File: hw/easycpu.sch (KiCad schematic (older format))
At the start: 0 parts

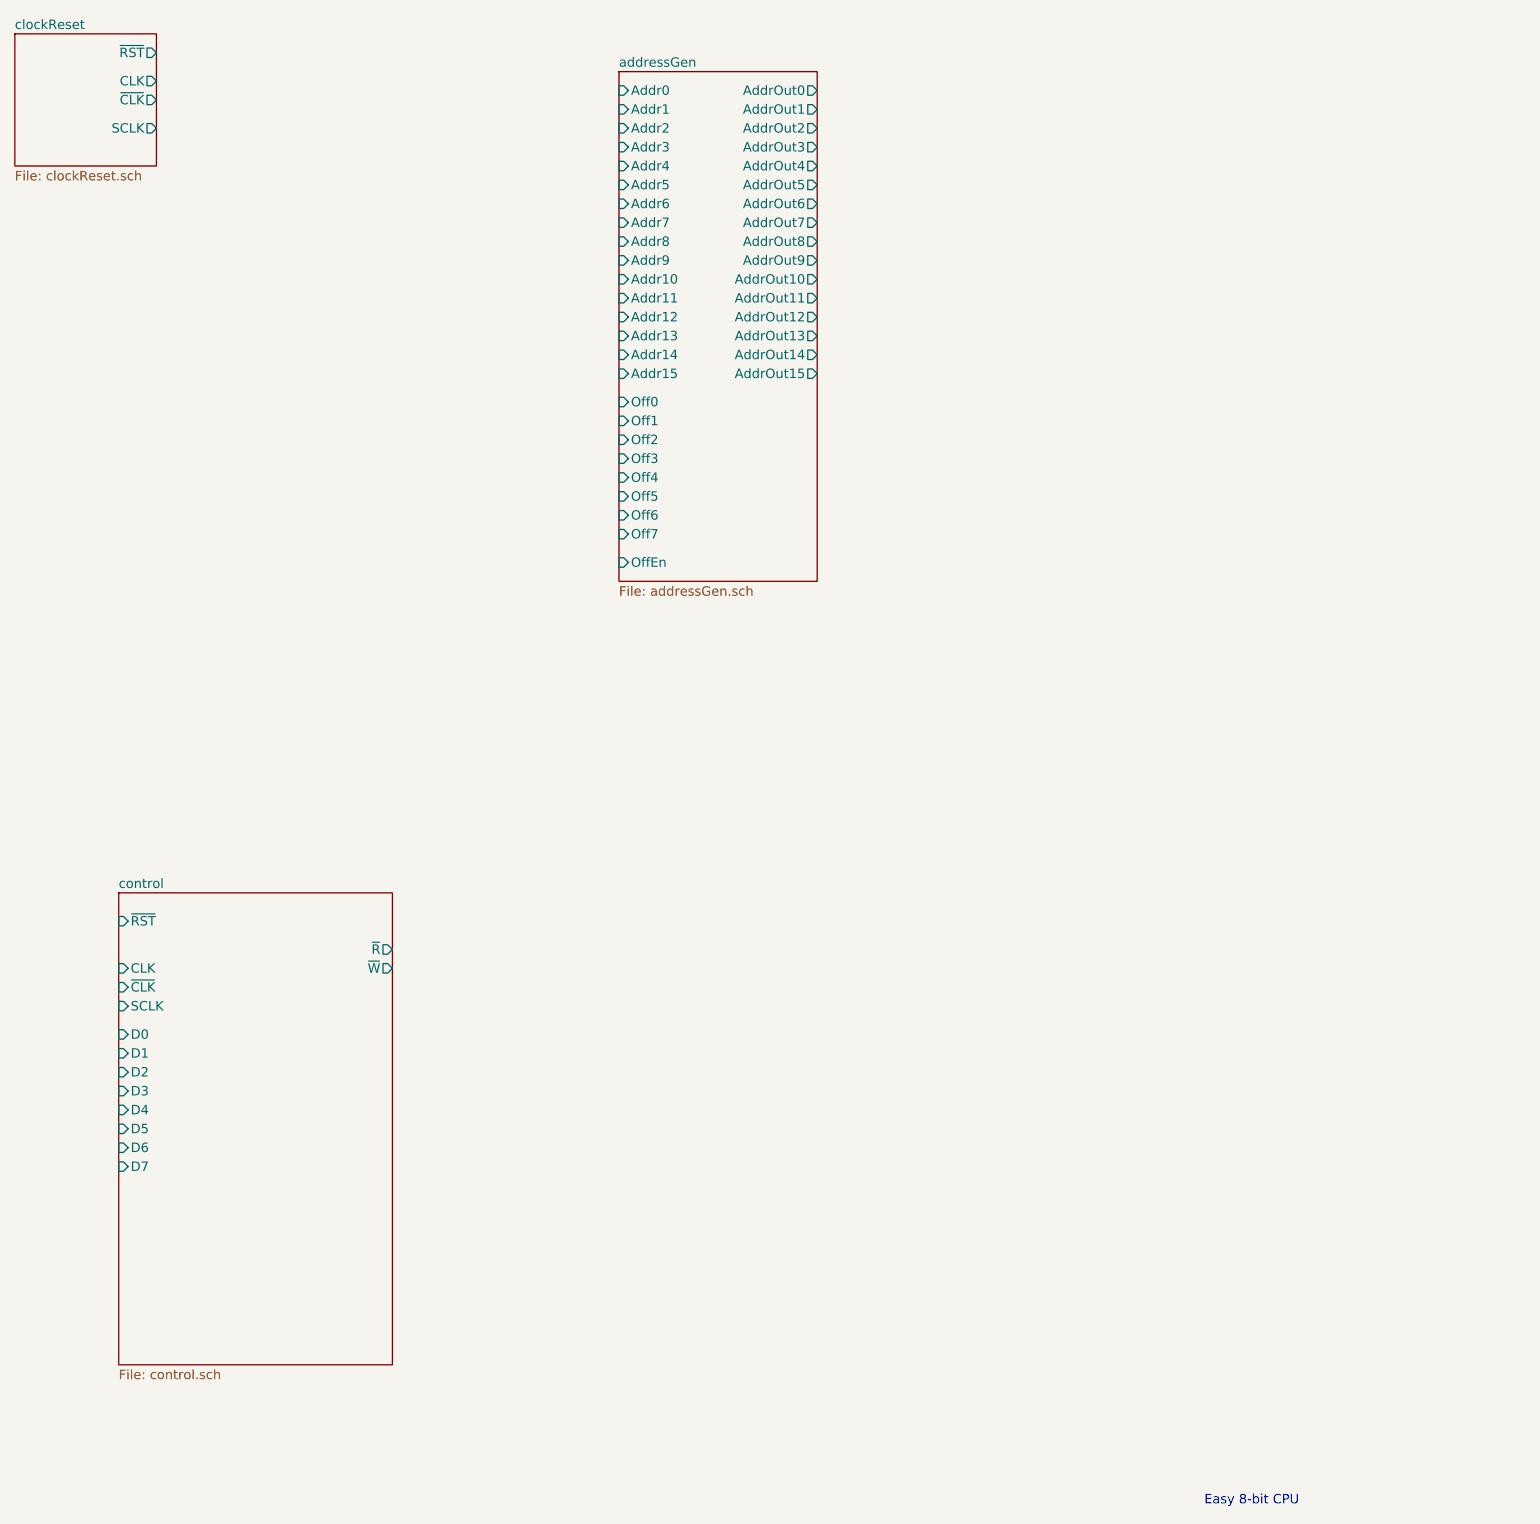
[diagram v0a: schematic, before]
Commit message: use '273 registers for ucode, initial PC design
The microcode registers need to be reset to a known
state on startup.  The 74HCT273 is appropriate for this.
One consequence is that all microcode signals must be
designed such that a 0 is the correct output for
coming out of reset: the main thing that needs to
happen is putting an initial value into the program
counter.  I'm assuming that a '541 buffer will
put an appropriate byte value (maybe 0xC0) on the
D bus on reset, and the PC can load this in both
bytes (so, effective initial PC of 0xC0C0).

Created an initial design for the program counter.
Used 74HC191 synchronous counters, with a 74HC10
triple 3-input NAND to enable counting for each 4
bits as appopriate based on the terminal count status
of the prior counters.
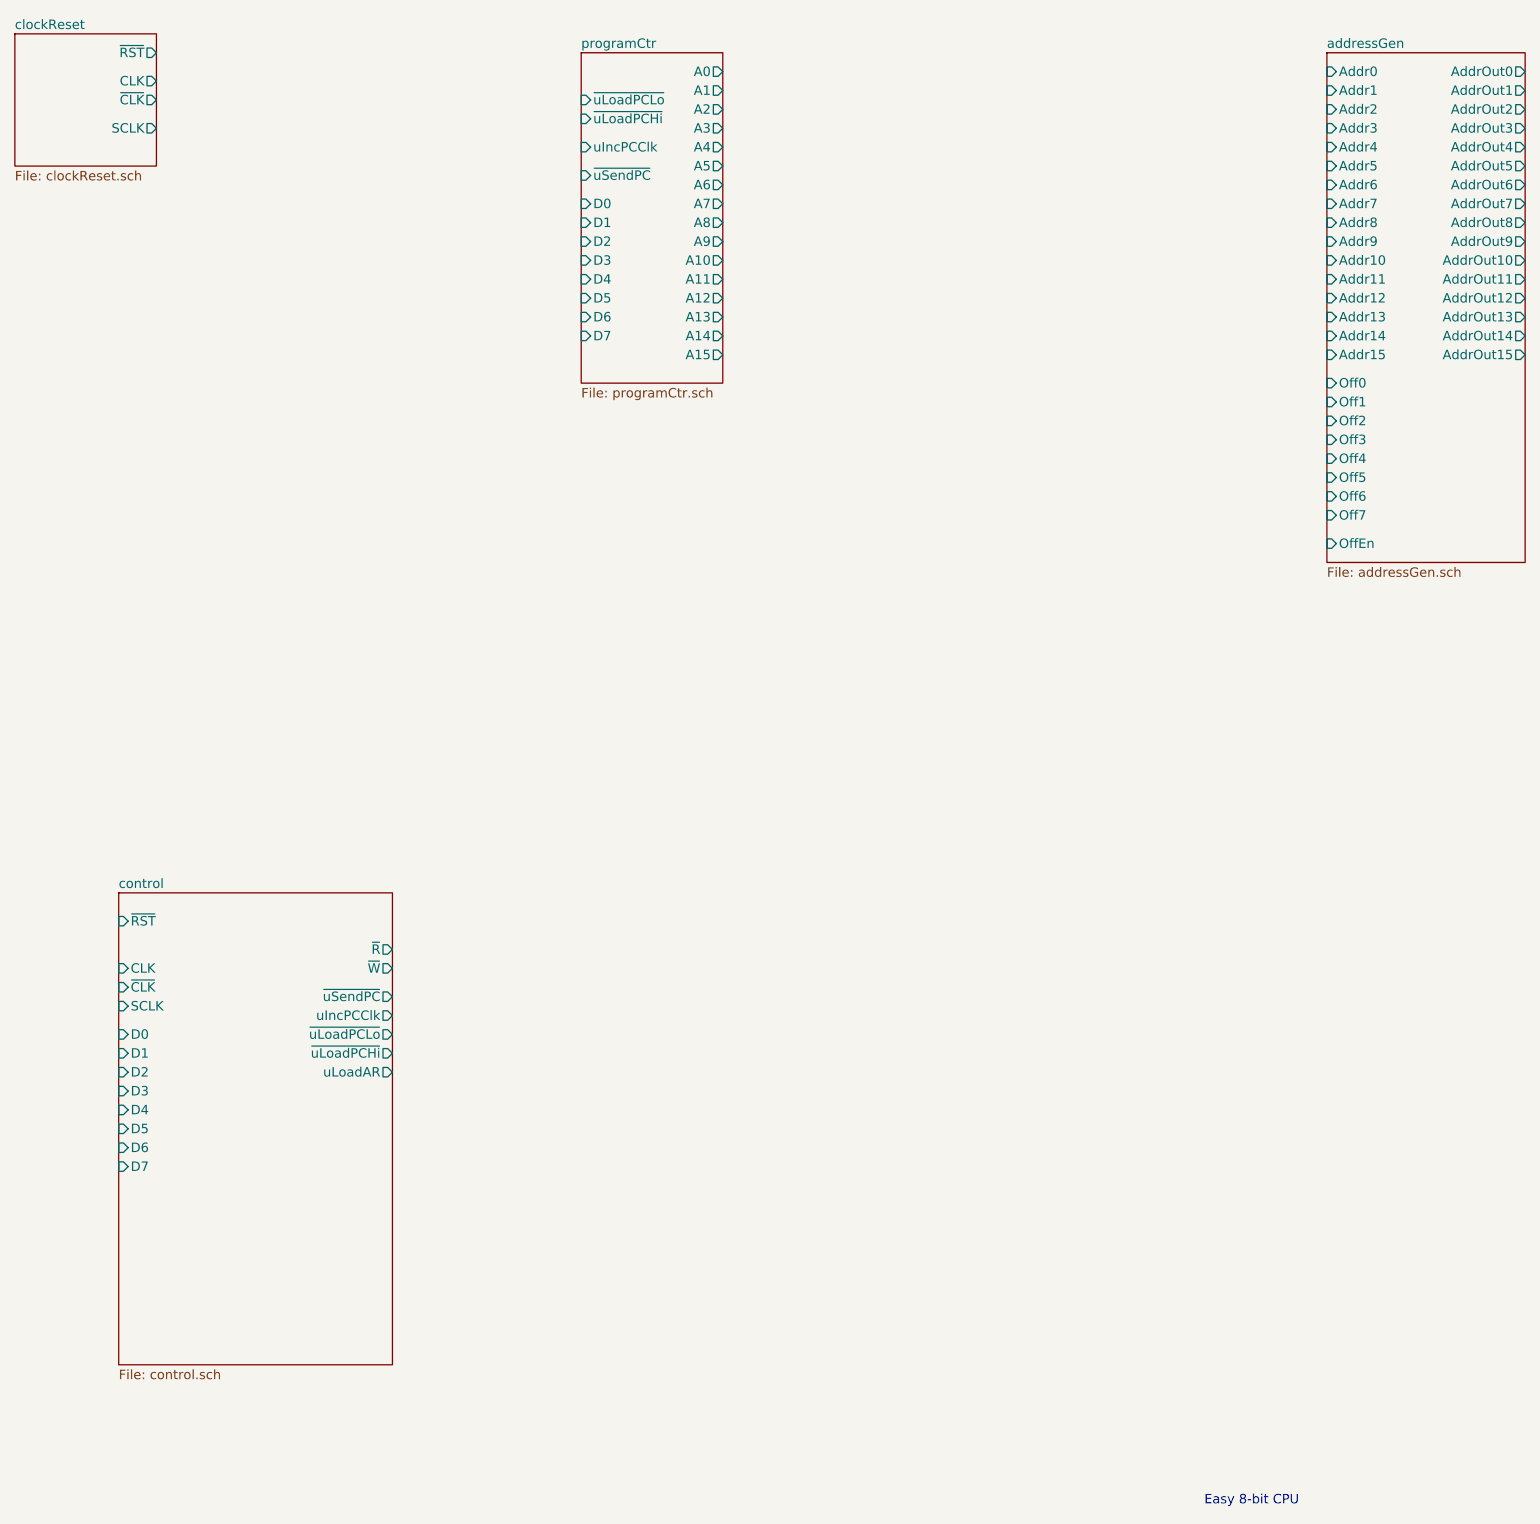
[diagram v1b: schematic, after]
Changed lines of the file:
@@
 EESchema Schematic File Version 4
 LIBS:easycpu-cache
-EELAYER 26 0
+EELAYER 30 0
 EELAYER END
 $Descr User 13750 10625
 encoding utf-8
-Sheet 1 4
+Sheet 1 5
 Title ""
 Date ""
@@
 $EndDescr
 $Sheet
-S 6000 1500 1050 2700
+S 9750 1400 1050 2700
 U 5D98FACA
 F0 "addressGen" 50
 F1 "addressGen.sch" 50
-F2 "Addr0" I L 6000 1600 50
-F3 "Addr1" I L 6000 1700 50
-F4 "Addr2" I L 6000 1800 50
-F5 "Addr3" I L 6000 1900 50
-F6 "Addr4" I L 6000 2000 50
-F7 "Addr5" I L 6000 2100 50
-F8 "Addr6" I L 6000 2200 50
-F9 "Addr7" I L 6000 2300 50
-F10 "Addr8" I L 6000 2400 50
-F11 "Addr9" I L 6000 2500 50
-F12 "Addr10" I L 6000 2600 50
-F13 "Addr11" I L 6000 2700 50
-F14 "Addr12" I L 6000 2800 50
-F15 "Addr13" I L 6000 2900 50
-F16 "Addr14" I L 6000 3000 50
-F17 "Addr15" I L 6000 3100 50
-F18 "Off0" I L 6000 3250 50
-F19 "Off1" I L 6000 3350 50
-F20 "Off2" I L 6000 3450 50
-F21 "Off3" I L 6000 3550 50
-F22 "Off4" I L 6000 3650 50
-F23 "Off5" I L 6000 3750 50
-F24 "Off6" I L 6000 3850 50
-F25 "Off7" I L 6000 3950 50
-F26 "OffEn" I L 6000 4100 50
-F27 "AddrOut0" O R 7050 1600 50
-F28 "AddrOut1" O R 7050 1700 50
-F29 "AddrOut2" O R 7050 1800 50
-F30 "AddrOut3" O R 7050 1900 50
-F31 "AddrOut4" O R 7050 2000 50
-F32 "AddrOut5" O R 7050 2100 50
-F33 "AddrOut6" O R 7050 2200 50
-F34 "AddrOut7" O R 7050 2300 50
-F35 "AddrOut8" O R 7050 2400 50
-F36 "AddrOut9" O R 7050 2500 50
-F37 "AddrOut10" O R 7050 2600 50
-F38 "AddrOut11" O R 7050 2700 50
-F39 "AddrOut12" O R 7050 2800 50
-F40 "AddrOut13" O R 7050 2900 50
-F41 "AddrOut14" O R 7050 3000 50
-F42 "AddrOut15" O R 7050 3100 50
+F2 "Addr0" I L 9750 1500 50
+F3 "Addr1" I L 9750 1600 50
+F4 "Addr2" I L 9750 1700 50
+F5 "Addr3" I L 9750 1800 50
+F6 "Addr4" I L 9750 1900 50
+F7 "Addr5" I L 9750 2000 50
+F8 "Addr6" I L 9750 2100 50
+F9 "Addr7" I L 9750 2200 50
+F10 "Addr8" I L 9750 2300 50
+F11 "Addr9" I L 9750 2400 50
+F12 "Addr10" I L 9750 2500 50
+F13 "Addr11" I L 9750 2600 50
+F14 "Addr12" I L 9750 2700 50
+F15 "Addr13" I L 9750 2800 50
+F16 "Addr14" I L 9750 2900 50
+F17 "Addr15" I L 9750 3000 50
+F18 "Off0" I L 9750 3150 50
+F19 "Off1" I L 9750 3250 50
+F20 "Off2" I L 9750 3350 50
+F21 "Off3" I L 9750 3450 50
+F22 "Off4" I L 9750 3550 50
+F23 "Off5" I L 9750 3650 50
+F24 "Off6" I L 9750 3750 50
+F25 "Off7" I L 9750 3850 50
+F26 "OffEn" I L 9750 4000 50
+F27 "AddrOut0" O R 10800 1500 50
+F28 "AddrOut1" O R 10800 1600 50
+F29 "AddrOut2" O R 10800 1700 50
+F30 "AddrOut3" O R 10800 1800 50
+F31 "AddrOut4" O R 10800 1900 50
+F32 "AddrOut5" O R 10800 2000 50
+F33 "AddrOut6" O R 10800 2100 50
+F34 "AddrOut7" O R 10800 2200 50
+F35 "AddrOut8" O R 10800 2300 50
+F36 "AddrOut9" O R 10800 2400 50
+F37 "AddrOut10" O R 10800 2500 50
+F38 "AddrOut11" O R 10800 2600 50
+F39 "AddrOut12" O R 10800 2700 50
+F40 "AddrOut13" O R 10800 2800 50
+F41 "AddrOut14" O R 10800 2900 50
+F42 "AddrOut15" O R 10800 3000 50
 $EndSheet
 Text Notes 9100 9100 0    50   ~ 0
@@
 F14 "CLK" I L 3350 6250 50
 F15 "~W" O R 4800 6250 50
+F16 "uLoadAR" O R 4800 6800 50
+F17 "~uSendPC" O R 4800 6400 50
+F18 "uIncPCClk" O R 4800 6500 50
+F19 "~uLoadPCLo" O R 4800 6600 50
+F20 "~uLoadPCHi" O R 4800 6700 50
 $EndSheet
 $Sheet
@@
 F5 "SCLK" O R 3550 1800 50
 $EndSheet
+$Sheet
+S 5800 1400 750  1750
+U 5DBB17DF
+F0 "programCtr" 50
+F1 "programCtr.sch" 50
+F2 "~uLoadPCLo" I L 5800 1650 50
+F3 "~uLoadPCHi" I L 5800 1750 50
+F4 "D0" I L 5800 2200 50
+F5 "D1" I L 5800 2300 50
+F6 "D2" I L 5800 2400 50
+F7 "D3" I L 5800 2500 50
+F8 "D4" I L 5800 2600 50
+F9 "D5" I L 5800 2700 50
+F10 "D6" I L 5800 2800 50
+F11 "D7" I L 5800 2900 50
+F12 "~uSendPC" I L 5800 2050 50
+F13 "A0" O R 6550 1500 50
+F14 "A1" O R 6550 1600 50
+F15 "A2" O R 6550 1700 50
+F16 "A3" O R 6550 1800 50
+F17 "A4" O R 6550 1900 50
+F18 "A5" O R 6550 2000 50
+F19 "A6" O R 6550 2100 50
+F20 "A7" O R 6550 2200 50
+F21 "A8" O R 6550 2300 50
+F22 "A9" O R 6550 2400 50
+F23 "A10" O R 6550 2500 50
+F24 "A11" O R 6550 2600 50
+F25 "A12" O R 6550 2700 50
+F26 "A13" O R 6550 2800 50
+F27 "A14" O R 6550 2900 50
+F28 "A15" O R 6550 3000 50
+F29 "uIncPCClk" I L 5800 1900 50
+$EndSheet
 $EndSCHEMATC

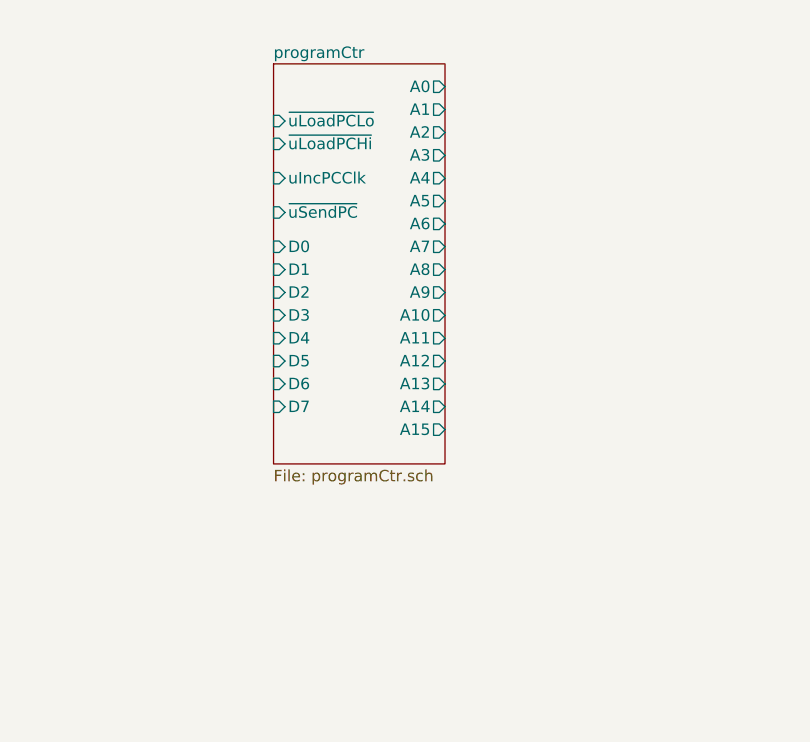
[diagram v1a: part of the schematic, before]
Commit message: program counter is now 2x 74HCT574
Increment is done using the address generation unit,
and the output of address generation can be optionally
sent back to the address registers (such as PC)
via buffers.

This hugely simplifies the program counter implementation,
and also makes it easy to provide additional address
registers (X, SP) that can benefit from increment
and decrement operations.
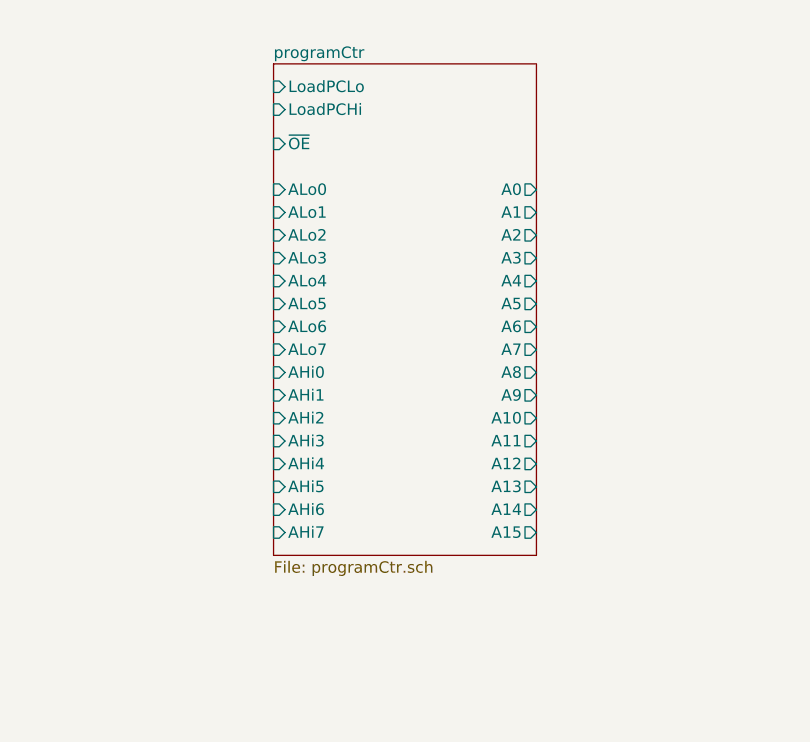
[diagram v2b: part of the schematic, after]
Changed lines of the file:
@@
 EESchema Schematic File Version 4
 LIBS:easycpu-cache
-EELAYER 30 0
+EELAYER 26 0
 EELAYER END
 $Descr User 13750 10625
@@
 $EndSheet
 $Sheet
-S 5800 1400 750  1750
+S 5800 1400 1150 2150
 U 5DBB17DF
 F0 "programCtr" 50
 F1 "programCtr.sch" 50
-F2 "~uLoadPCLo" I L 5800 1650 50
-F3 "~uLoadPCHi" I L 5800 1750 50
-F4 "D0" I L 5800 2200 50
-F5 "D1" I L 5800 2300 50
-F6 "D2" I L 5800 2400 50
-F7 "D3" I L 5800 2500 50
-F8 "D4" I L 5800 2600 50
-F9 "D5" I L 5800 2700 50
-F10 "D6" I L 5800 2800 50
-F11 "D7" I L 5800 2900 50
-F12 "~uSendPC" I L 5800 2050 50
-F13 "A0" O R 6550 1500 50
-F14 "A1" O R 6550 1600 50
-F15 "A2" O R 6550 1700 50
-F16 "A3" O R 6550 1800 50
-F17 "A4" O R 6550 1900 50
-F18 "A5" O R 6550 2000 50
-F19 "A6" O R 6550 2100 50
-F20 "A7" O R 6550 2200 50
-F21 "A8" O R 6550 2300 50
-F22 "A9" O R 6550 2400 50
-F23 "A10" O R 6550 2500 50
-F24 "A11" O R 6550 2600 50
-F25 "A12" O R 6550 2700 50
-F26 "A13" O R 6550 2800 50
-F27 "A14" O R 6550 2900 50
-F28 "A15" O R 6550 3000 50
-F29 "uIncPCClk" I L 5800 1900 50
+F2 "A0" O R 6950 1950 50
+F3 "A1" O R 6950 2050 50
+F4 "A2" O R 6950 2150 50
+F5 "A3" O R 6950 2250 50
+F6 "A4" O R 6950 2350 50
+F7 "A5" O R 6950 2450 50
+F8 "A6" O R 6950 2550 50
+F9 "A7" O R 6950 2650 50
+F10 "A8" O R 6950 2750 50
+F11 "A9" O R 6950 2850 50
+F12 "A10" O R 6950 2950 50
+F13 "A11" O R 6950 3050 50
+F14 "A12" O R 6950 3150 50
+F15 "A13" O R 6950 3250 50
+F16 "A14" O R 6950 3350 50
+F17 "A15" O R 6950 3450 50
+F18 "ALo0" I L 5800 1950 50
+F19 "ALo1" I L 5800 2050 50
+F20 "ALo2" I L 5800 2150 50
+F21 "ALo3" I L 5800 2250 50
+F22 "ALo4" I L 5800 2350 50
+F23 "ALo5" I L 5800 2450 50
+F24 "ALo6" I L 5800 2550 50
+F25 "ALo7" I L 5800 2650 50
+F26 "AHi0" I L 5800 2750 50
+F27 "AHi1" I L 5800 2850 50
+F28 "AHi2" I L 5800 2950 50
+F29 "AHi3" I L 5800 3050 50
+F30 "AHi4" I L 5800 3150 50
+F31 "AHi5" I L 5800 3250 50
+F32 "AHi6" I L 5800 3350 50
+F33 "AHi7" I L 5800 3450 50
+F34 "LoadPCLo" I L 5800 1500 50
+F35 "LoadPCHi" I L 5800 1600 50
+F36 "~OE" I L 5800 1750 50
 $EndSheet
 $EndSCHEMATC
